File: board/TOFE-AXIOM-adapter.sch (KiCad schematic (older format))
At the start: 21 parts, among them CN1 C, U1 24AA01/24LC01B, U2 LM317T, U3 LM7805CT

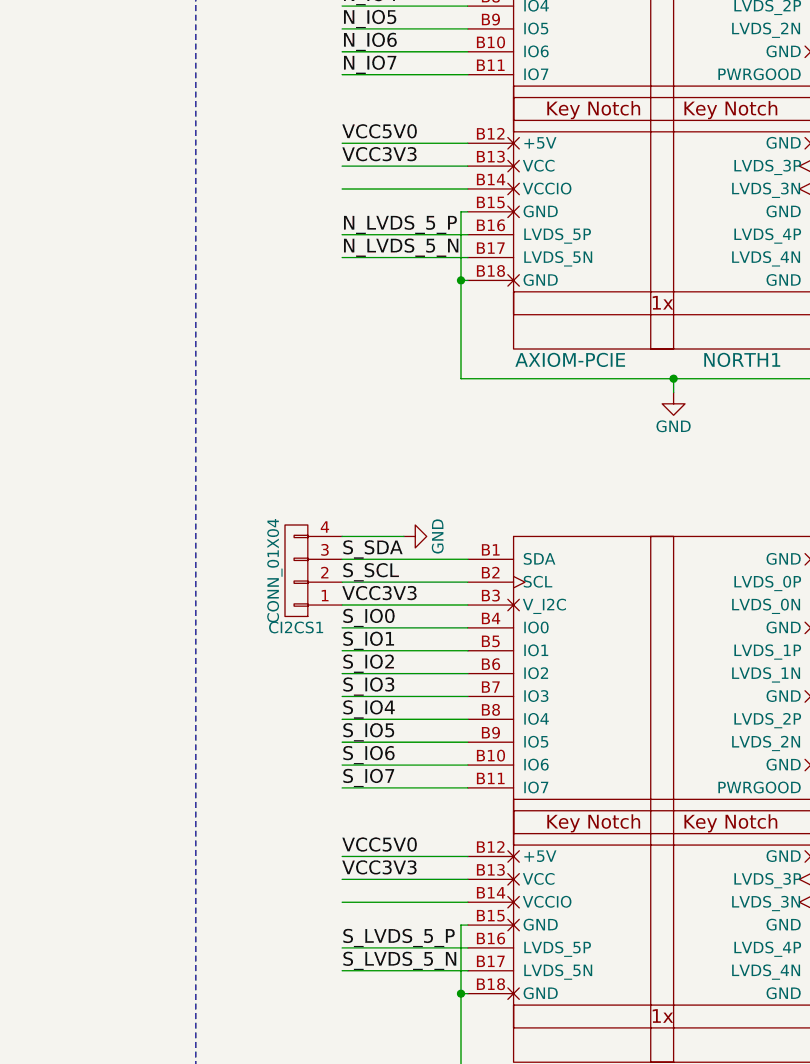
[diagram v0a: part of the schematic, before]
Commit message: Setting VCCIO to VCC3V3.
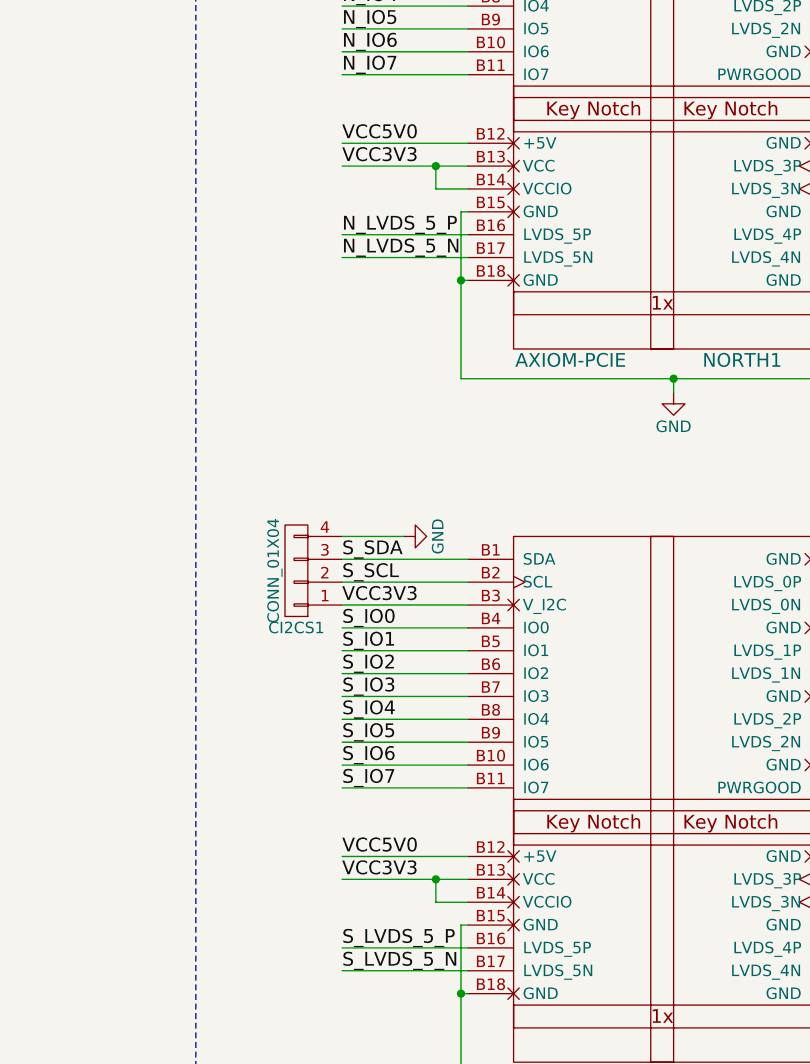
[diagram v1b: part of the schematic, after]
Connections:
- wire segments 237 -> 239

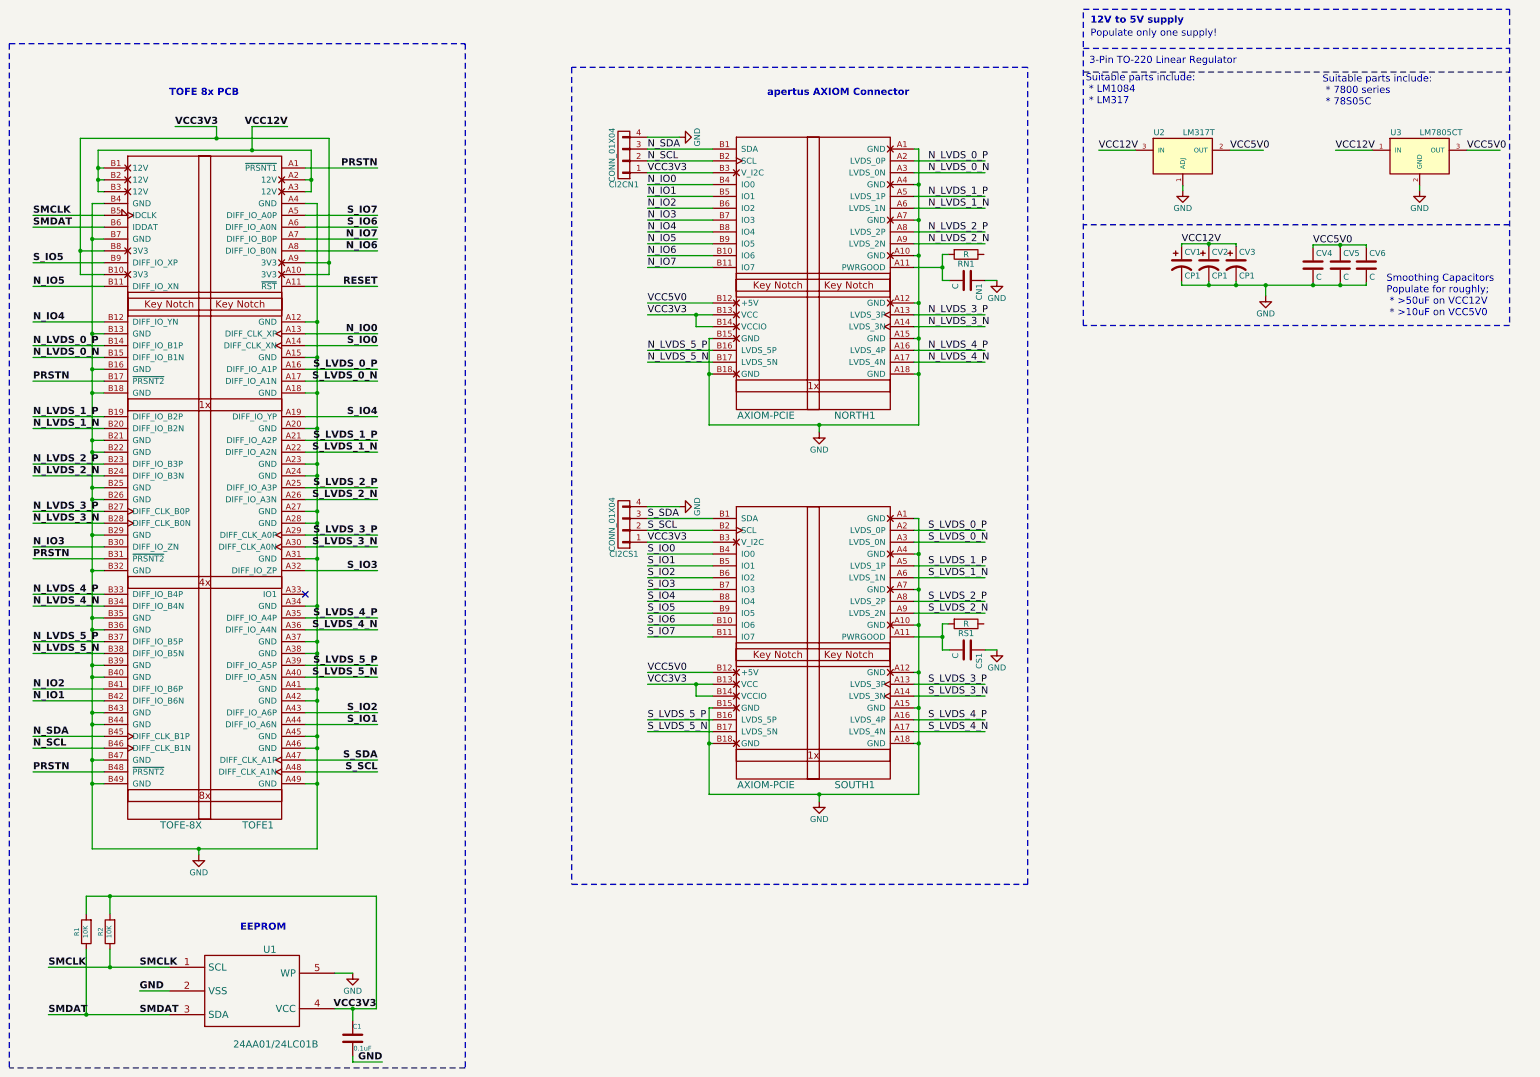
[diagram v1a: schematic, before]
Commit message: Fix pullup PWRGOOD circuit.
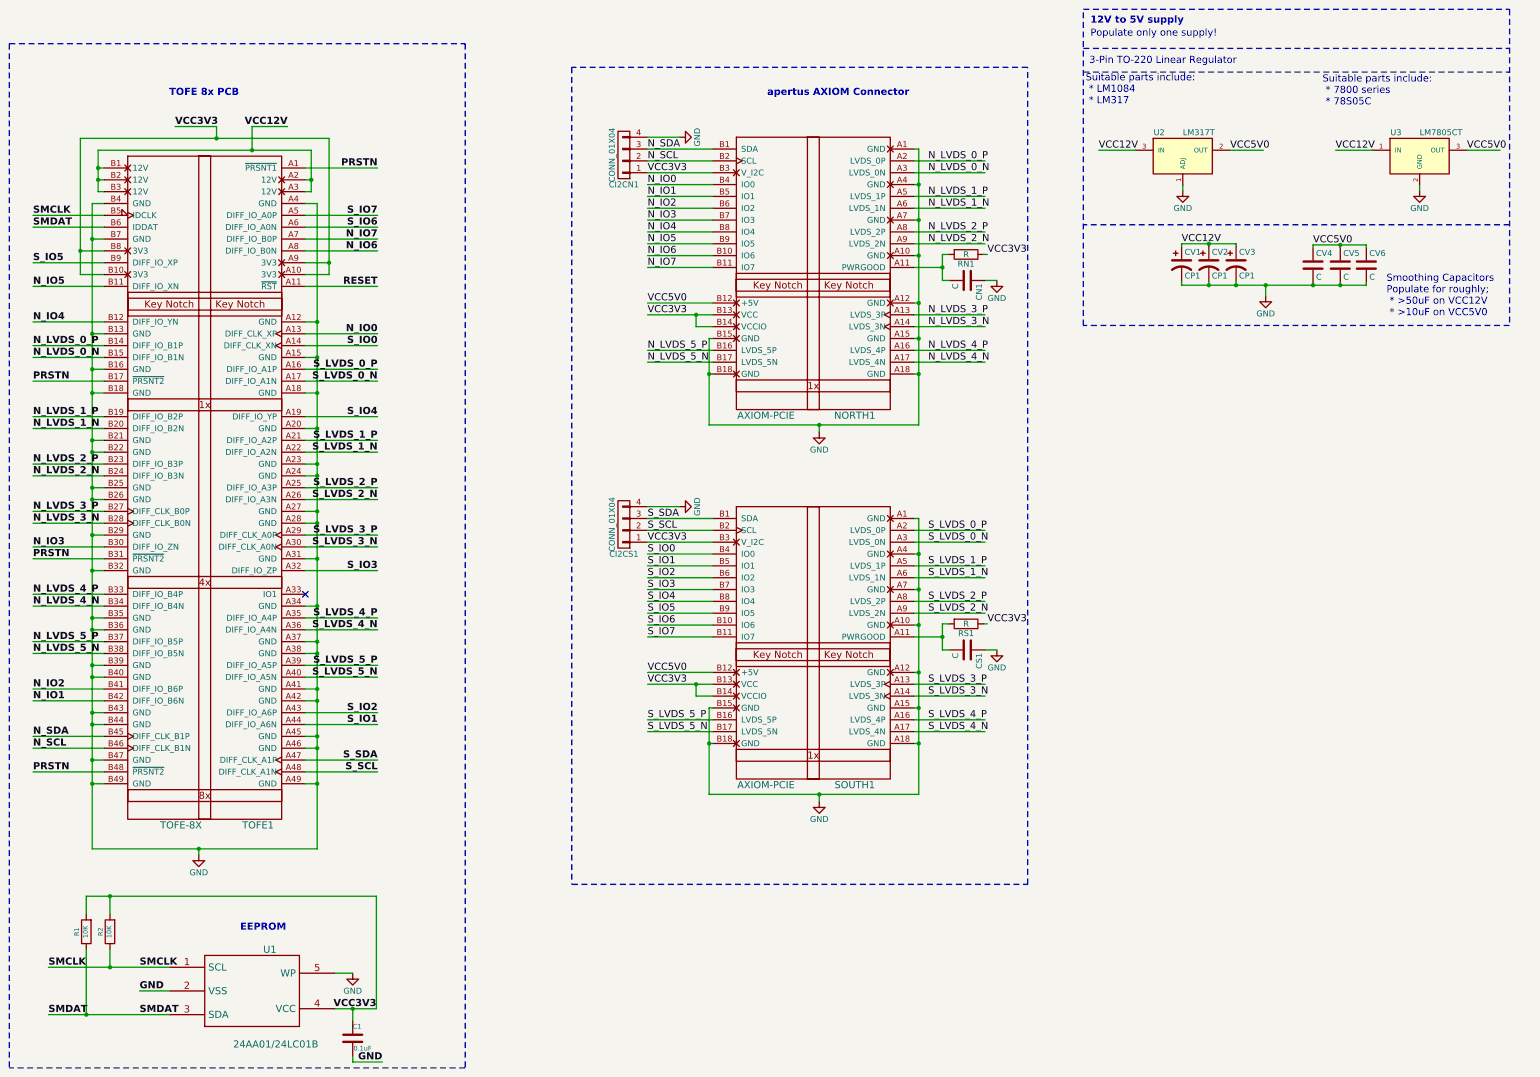
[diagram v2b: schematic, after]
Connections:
- wire segments 239 -> 241
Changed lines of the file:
@@
 	5600 2850 5700 2850
 Wire Wire Line
-	5700 2850 5700 8300
+	5700 8300 5700 2850
 Wire Wire Line
 	5700 4150 5600 4150
@@
 Connection ~ 5700 7450
 Wire Wire Line
-	5700 8300 3800 8300
+	3800 8300 5700 8300
 Connection ~ 3800 7750
 Connection ~ 5700 7750
@@
 	9040 3390 8490 3390
 Wire Wire Line
-	9040 3790 8490 3790
+	8490 3790 9040 3790
 Wire Wire Line
 	9040 4090 8490 4090
@@
 	10740 2390 10780 2390
 Wire Wire Line
-	10780 2390 10780 4720
+	10780 4720 10780 2390
 Wire Wire Line
 	10740 2690 10780 2690
@@
 Connection ~ 10780 3690
 Wire Wire Line
-	10780 4720 9010 4720
+	9010 4720 10780 4720
 Connection ~ 10780 4290
 Wire Wire Line
 	9040 4290 9010 4290
 Wire Wire Line
-	9010 4720 9010 3990
+	9010 3990 9010 4720
 Wire Wire Line
 	9010 3990 9040 3990
@@
 	9040 6510 8490 6510
 Wire Wire Line
-	9040 6910 8490 6910
+	8490 6910 9040 6910
 Wire Wire Line
 	9040 7210 8490 7210
@@
 	10740 5510 10780 5510
 Wire Wire Line
-	10780 5510 10780 7840
+	10780 7840 10780 5510
 Wire Wire Line
 	10740 5810 10780 5810
@@
 Connection ~ 10780 6810
 Wire Wire Line
-	10780 7840 9010 7840
+	9010 7840 10780 7840
 Connection ~ 10780 7410
 Wire Wire Line
 	9040 7410 9010 7410
 Wire Wire Line
-	9010 7840 9010 7110
+	9010 7110 9010 7840
 Wire Wire Line
 	9010 7110 9040 7110
@@
 Wire Wire Line
 	9040 7010 8900 7010
+Wire Wire Line
+	11330 3280 11360 3280
+Wire Wire Line
+	11330 6400 11360 6400
+Text Label 11360 6400 0    60   ~ 0
+VCC3V3
+Text Label 11360 3280 0    60   ~ 0
+VCC3V3
 $EndSCHEMATC

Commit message: Update number 3 from Phyllis.
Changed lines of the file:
@@
 	5600 2850 5700 2850
 Wire Wire Line
-	5700 8300 5700 2850
+	5700 2850 5700 8300
 Wire Wire Line
 	5700 4150 5600 4150
@@
 Connection ~ 5700 7450
 Wire Wire Line
-	3800 8300 5700 8300
+	5700 8300 3800 8300
 Connection ~ 3800 7750
 Connection ~ 5700 7750
@@
 	10740 2390 10780 2390
 Wire Wire Line
-	10780 4720 10780 2390
+	10780 2390 10780 4720
 Wire Wire Line
 	10740 2690 10780 2690
@@
 Connection ~ 10780 3690
 Wire Wire Line
-	9010 4720 10780 4720
+	10780 4720 9010 4720
 Connection ~ 10780 4290
 Wire Wire Line
 	9040 4290 9010 4290
 Wire Wire Line
-	9010 3990 9010 4720
+	9010 4720 9010 3990
 Wire Wire Line
 	9010 3990 9040 3990
@@
 	10740 5510 10780 5510
 Wire Wire Line
-	10780 7840 10780 5510
+	10780 5510 10780 7840
 Wire Wire Line
 	10740 5810 10780 5810
@@
 Connection ~ 10780 6810
 Wire Wire Line
-	9010 7840 10780 7840
+	10780 7840 9010 7840
 Connection ~ 10780 7410
 Wire Wire Line
 	9040 7410 9010 7410
 Wire Wire Line
-	9010 7110 9010 7840
+	9010 7840 9010 7110
 Wire Wire Line
 	9010 7110 9040 7110
